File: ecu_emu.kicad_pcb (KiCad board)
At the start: 2 copper layers, 51.3 x 16.5 mm, 34 parts, among them J1 Conn_02x06_Odd_Even, J2 Conn_01x04_Male, U1 LD1117S33TR_SOT223, U2 STM32F105RBTx, U3 BSP742R, U4 E-L9637D, Y1 Crystal KX-9A

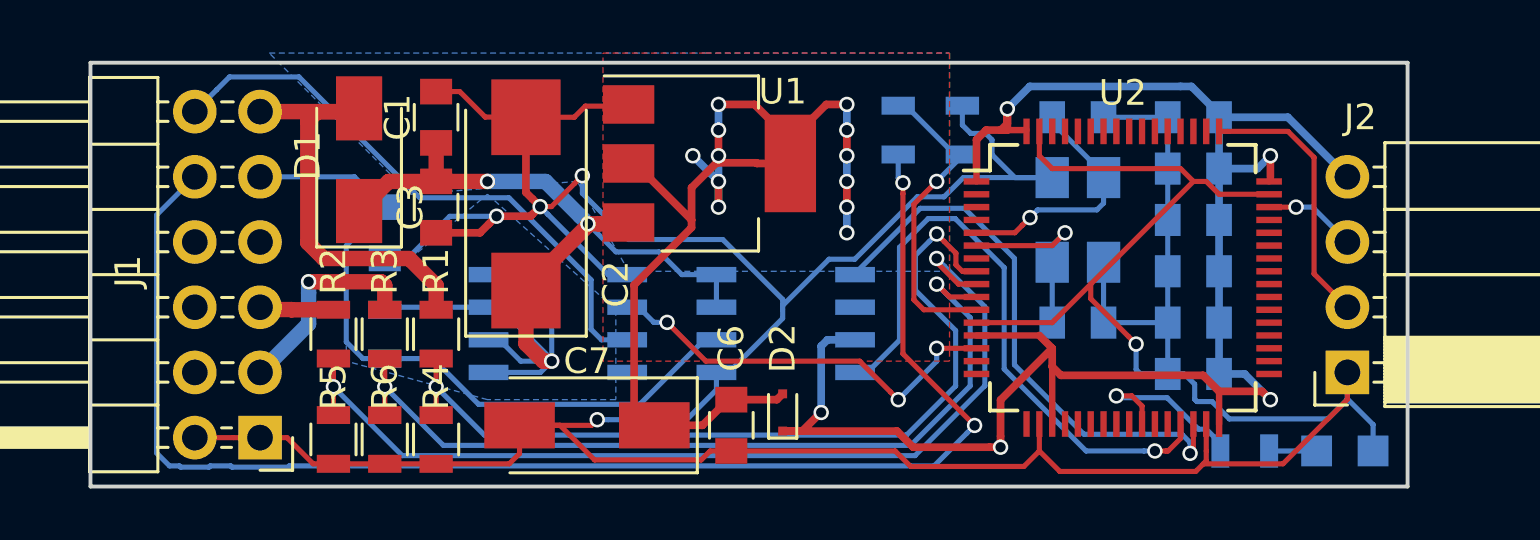
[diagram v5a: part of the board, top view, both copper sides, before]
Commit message: more fixes 1. separate power on k-bus IC logic 2. D2 change to shottky diod 3. pull-up on stm RESET pin 4. change linier stabilizer to adjastable version, to make apropriate voltage on stm throw diod
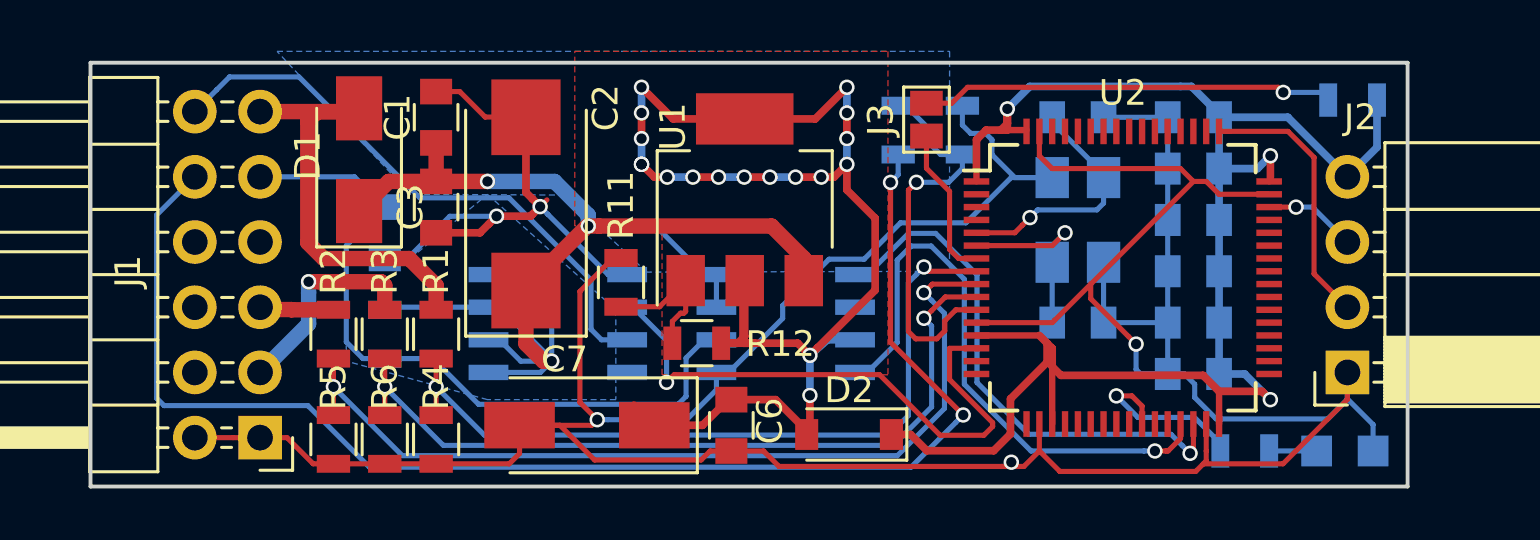
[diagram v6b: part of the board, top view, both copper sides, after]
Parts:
- added J3: GS2, Connectors:GS2, F.Cu at (60.6, 23.1)
- added R11: 240, Resistors_SMD:R_0805, F.Cu at (48.7, 29.4)
- added R12: 120, Resistors_SMD:R_0805, F.Cu at (51.7, 31.8)
- added R13: 100k, Resistors_SMD:R_0805, B.Cu at (77.2, 22.3)
- D2: value PMLL4148L.115 -> 1N5819HW-7-F; footprint Diodes_SMD:D_SC-80 -> Diodes_SMD:D_SOD-123
- U1: value LD1117S33TR_SOT223 -> AMS1117-ADJ
- moved D2 2.72 mm to (57.6, 35.4), turned to 180 degrees
- moved U1 1.97 mm to (53.5, 26.2), turned to 90 degrees
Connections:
- J1 pad 4: /ECU_P/N -> (no net)
- J1 pad 6: Net-(J1-Pad6) -> (no net)
- J1 pad 7: Net-(J1-Pad7) -> (no net)
- J1 pad 8: /Transmission_control_module -> (no net)
- U1 pad 1: GND -> Net-(R11-Pad1)
- U2 pad 15: Net-(U2-Pad15) -> (no net)
- U2 pad 16: Net-(U2-Pad16) -> (no net)
- U2 pad 17: Net-(U2-Pad17) -> (no net)
- U2 pad 2: Net-(U2-Pad2) -> (no net)
- U2 pad 20: Net-(U2-Pad20) -> (no net)
- U2 pad 21: Net-(U2-Pad21) -> (no net)
- U2 pad 22: Net-(U2-Pad22) -> (no net)
- U2 pad 23: Net-(U2-Pad23) -> (no net)
- U2 pad 24: Net-(U2-Pad24) -> (no net)
- U2 pad 25: Net-(U2-Pad25) -> (no net)
- U2 pad 27: Net-(U2-Pad27) -> (no net)
- U2 pad 28: Net-(U2-Pad28) -> (no net)
- U2 pad 3: Net-(U2-Pad3) -> (no net)
- U2 pad 33: Net-(U2-Pad33) -> (no net)
- U2 pad 34: Net-(U2-Pad34) -> (no net)
- U2 pad 35: Net-(U2-Pad35) -> (no net)
- U2 pad 36: Net-(U2-Pad36) -> (no net)
- U2 pad 37: Net-(U2-Pad37) -> (no net)
- U2 pad 38: Net-(U2-Pad38) -> (no net)
- U2 pad 39: Net-(U2-Pad39) -> (no net)
- U2 pad 4: Net-(U2-Pad4) -> (no net)
- U2 pad 40: Net-(U2-Pad40) -> (no net)
- U2 pad 41: Net-(U2-Pad41) -> (no net)
- U2 pad 42: Net-(U2-Pad42) -> (no net)
- U2 pad 43: Net-(U2-Pad43) -> (no net)
- U2 pad 44: Net-(U2-Pad44) -> (no net)
- U2 pad 45: Net-(U2-Pad45) -> (no net)
- U2 pad 50: Net-(U2-Pad50) -> (no net)
- U2 pad 51: Net-(U2-Pad51) -> (no net)
- U2 pad 52: Net-(U2-Pad52) -> (no net)
- U2 pad 53: Net-(U2-Pad53) -> (no net)
- U2 pad 54: Net-(U2-Pad54) -> (no net)
- U2 pad 55: Net-(U2-Pad55) -> (no net)
- U2 pad 56: Net-(U2-Pad56) -> (no net)
- U2 pad 57: Net-(U2-Pad57) -> (no net)
- U2 pad 58: Net-(U2-Pad58) -> (no net)
- U2 pad 59: Net-(U2-Pad59) -> (no net)
- U2 pad 60: Net-(U2-Pad60) -> (no net)
- U2 pad 61: Net-(U2-Pad61) -> (no net)
- U2 pad 62: Net-(U2-Pad62) -> (no net)
- U2 pad 7: Net-(U2-Pad7) -> /NRST
- U3 pad 4: Net-(U3-Pad4) -> (no net)
- U4 pad 2: Net-(U4-Pad2) -> (no net)
- U4 pad 3: /+3V3_STM -> /+3V3
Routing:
- net Net-(J3-Pad2): track 0.00 -> 16.1 mm, vias 0 -> 1
- net /+3V3: track 42.1 -> 55.4 mm, vias 12 -> 18
- net GND: track 179.6 -> 171.0 mm
- net /Kbus_Vbatt: track 44.8 -> 53.2 mm
- net /+3V3_STM: track 72.9 -> 66.4 mm, vias 5 -> 3
- net /solenoid_driver: track 16.2 -> 22.4 mm, vias 3 -> 1
- net Net-(R11-Pad1): track 0.00 -> 6.14 mm
- net /NRST: track 0.00 -> 5.98 mm
- net /ADC_Vbatt: track 33.3 -> 29.8 mm
- net Net-(R7-Pad1): track 12.3 -> 15.6 mm
- net /ADC_IGN: track 37.6 -> 34.9 mm
- net /ADC_AUX: track 33.2 -> 31.0 mm
- net /ECU_HALL_sensor+: track 56.0 -> 54.1 mm
- net /stm2Kbus_UART_RX: track 22.0 -> 20.9 mm
- net /stm2Kbus_UART_TX: track 24.1 -> 23.1 mm
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
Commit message: fix some, update gerbers
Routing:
- net /solenoid_driver: track 22.4 -> 23.2 mm
- net GND: track 171.0 -> 171.7 mm
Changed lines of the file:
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@@
     (thickness 1.6)
     (drawings 10)
-    (tracks 492)
+    (tracks 500)
     (zones 0)
     (modules 38)
@@
     (last_trace_width 0.2)
     (trace_clearance 0.2)
-    (zone_clearance 0.4)
+    (zone_clearance 0.45)
     (zone_45_only yes)
     (trace_min 0.1)
@@
       (padsonsilk false)
       (subtractmaskfromsilk false)
-      (outputformat 4)
+      (outputformat 1)
       (mirror false)
       (drillshape 0)
@@
   (gr_line (start 28.036 20.875) (end 79.344 20.875) (layer Edge.Cuts) (width 0.15))
   (gr_line (start 28.036 37.385) (end 28.036 20.875) (layer Edge.Cuts) (width 0.15))
+  (segment (start 34.64 35.48) (end 35.929969 35.48) (width 0.2) (layer F.Cu) (net 1))
+  (segment (start 35.929969 35.48) (end 36.17916 35.729191) (width 0.2) (layer F.Cu) (net 1))
+  (segment (start 36.17916 35.729191) (end 36.17916 36.374) (width 0.2) (layer F.Cu) (net 1))
+  (segment (start 36.30516 36.5) (end 37.5 36.5) (width 0.2) (layer F.Cu) (net 1))
+  (segment (start 36.17916 36.374) (end 36.30516 36.5) (width 0.2) (layer F.Cu) (net 1))
+  (segment (start 48.702 28.482) (end 48.702 29.256) (width 0.2) (layer F.Cu) (net 1))
+  (segment (start 48.702 29.256) (end 48.501436 29.456564) (width 0.2) (layer F.Cu) (net 1))
+  (segment (start 48.501436 29.456564) (end 47.788188 29.456564) (width 0.2) (layer F.Cu) (net 1))
+  (segment (start 47.788188 29.456564) (end 47.102 30.142752) (width 0.2) (layer F.Cu) (net 1))
+  (segment (start 47.102 30.142752) (end 47.102 34.107267) (width 0.2) (layer F.Cu) (net 1))
+  (segment (start 47.102 34.107267) (end 47.776239 34.781506) (width 0.2) (layer F.Cu) (net 1))
   (segment (start 63.502 36.603056) (end 64.396944 36.603056) (width 0.2) (layer F.Cu) (net 1))
   (segment (start 54.859656 36.603056) (end 63.502 36.603056) (width 0.2) (layer F.Cu) (net 1))
@@
   (segment (start 62.137598 27.112716) (end 63.902 25.348314) (width 0.2) (layer B.Cu) (net 1))
   (segment (start 65.498314 25.348314) (end 65.5 25.35) (width 0.2) (layer B.Cu) (net 1))
-  (segment (start 47.102 29.782) (end 47.102 34.107267) (width 0.2) (layer F.Cu) (net 1))
-  (segment (start 48.402 28.482) (end 47.102 29.782) (width 0.2) (layer F.Cu) (net 1))
-  (segment (start 47.102 34.107267) (end 47.776239 34.781506) (width 0.2) (layer F.Cu) (net 1))
-  (segment (start 48.702 28.482) (end 48.402 28.482) (width 0.2) (layer F.Cu) (net 1))
   (segment (start 77 32.94) (end 77 33.99) (width 0.2) (layer B.Cu) (net 1))
   (segment (start 77 33.99) (end 76.239037 34.750963) (width 0.2) (layer B.Cu) (net 1))
@@
   (segment (start 44.991758 22.991758) (end 45 23) (width 0.2) (layer F.Cu) (net 1))
   (segment (start 43.412329 22.991758) (end 44.991758 22.991758) (width 0.2) (layer F.Cu) (net 1))
-  (segment (start 34.64 35.48) (end 35.69 35.48) (width 0.2) (layer F.Cu) (net 1))
-  (segment (start 35.69 35.48) (end 36.71 36.5) (width 0.2) (layer F.Cu) (net 1))
-  (segment (start 36.71 36.5) (end 37.5 36.5) (width 0.2) (layer F.Cu) (net 1))
   (segment (start 71 25.5) (end 67 29.5) (width 0.2) (layer F.Cu) (net 1))
   (segment (start 67 29.5) (end 65.600009 30.899991) (width 0.2) (layer F.Cu) (net 1))
@@
   (segment (start 34.64 22.78) (end 38.373 22.78) (width 0.6) (layer F.Cu) (net 6))
   (segment (start 38.373 22.78) (end 38.5 22.653) (width 0.6) (layer F.Cu) (net 6))
+  (segment (start 63.752992 22.672254) (end 63.752992 23.24967) (width 0.3) (layer F.Cu) (net 7))
+  (segment (start 63.752992 23.24967) (end 63.502662 23.5) (width 0.3) (layer F.Cu) (net 7))
+  (segment (start 63.502662 23.5) (end 63.5 23.5) (width 0.3) (layer F.Cu) (net 7))
   (segment (start 78.152 22.332) (end 78.152 24.168) (width 0.3) (layer B.Cu) (net 7))
   (segment (start 78.152 24.168) (end 77 25.32) (width 0.3) (layer B.Cu) (net 7))
@@
   (segment (start 74.68 23) (end 72 23) (width 0.3) (layer B.Cu) (net 7))
   (segment (start 63.5 23.5) (end 64.5 23.5) (width 0.25) (layer F.Cu) (net 7))
-  (segment (start 63.752992 23.247008) (end 63.5 23.5) (width 0.3) (layer F.Cu) (net 7))
-  (segment (start 63.752992 22.672254) (end 63.752992 23.247008) (width 0.3) (layer F.Cu) (net 7))
   (segment (start 72 33) (end 72.997452 33) (width 0.3) (layer B.Cu) (net 7))
   (segment (start 72.997452 33) (end 73.998414 34.000962) (width 0.3) (layer B.Cu) (net 7))
@@
   (segment (start 62.55 30.5) (end 61.747516 30.5) (width 0.2) (layer F.Cu) (net 16))
   (segment (start 59.5 22.55) (end 59.8 22.55) (width 0.2) (layer B.Cu) (net 16))
-  (segment (start 61.5 32) (end 61.5 33.215499) (width 0.2) (layer F.Cu) (net 17))
-  (segment (start 61.5 33.215499) (end 63.180829 34.896328) (width 0.2) (layer F.Cu) (net 17))
+  (segment (start 63.180829 34.896328) (end 63.180829 35.046608) (width 0.2) (layer F.Cu) (net 17))
   (segment (start 63.180829 35.046608) (end 62.838522 35.388915) (width 0.2) (layer F.Cu) (net 17))
+  (segment (start 62.118501 33.834) (end 63.180829 34.896328) (width 0.2) (layer F.Cu) (net 17))
+  (segment (start 60.888 32.818) (end 61.904 33.834) (width 0.2) (layer F.Cu) (net 17))
+  (segment (start 61.198 32) (end 60.888 32.31) (width 0.2) (layer F.Cu) (net 17))
+  (segment (start 60.888 32.31) (end 60.888 32.818) (width 0.2) (layer F.Cu) (net 17))
+  (segment (start 62.55 32) (end 61.198 32) (width 0.2) (layer F.Cu) (net 17))
+  (segment (start 61.904 33.834) (end 62.118501 33.834) (width 0.2) (layer F.Cu) (net 17))
   (segment (start 50.776469 33.025666) (end 50.47647 33.325665) (width 0.2) (layer F.Cu) (net 17))
-  (segment (start 63.180829 34.896328) (end 63.180829 35.046608) (width 0.2) (layer F.Cu) (net 17))
   (segment (start 62.838522 35.388915) (end 61.133893 35.388915) (width 0.2) (layer F.Cu) (net 17))
   (segment (start 61.133893 35.388915) (end 58.770644 33.025666) (width 0.2) (layer F.Cu) (net 17))
@@
   (via (at 50.47647 33.325665) (size 0.6) (drill 0.4) (layers F.Cu B.Cu) (net 17))
   (segment (start 49.177561 30.4) (end 50.47647 31.698909) (width 0.2) (layer B.Cu) (net 17))
-  (segment (start 61.5 32) (end 62.55 32) (width 0.2) (layer F.Cu) (net 17))
   (segment (start 45 29.625) (end 47.386584 27.238416) (width 0.6) (layer F.Cu) (net 18))
   (segment (start 45 29.75) (end 45 29.625) (width 0.6) (layer F.Cu) (net 18))
@@
   (segment (start 39.653 25.5) (end 38.5 26.653) (width 0.6) (layer F.Cu) (net 18))
   (segment (start 41.5 24) (end 41.5 25.5) (width 0.6) (layer F.Cu) (net 18))
+  (segment (start 38 28) (end 39.5 26.5) (width 0.2) (layer B.Cu) (net 19))
+  (segment (start 38 31.75) (end 38 28) (width 0.2) (layer B.Cu) (net 19))
+  (segment (start 38.65 32.4) (end 38 31.75) (width 0.2) (layer B.Cu) (net 19))
+  (segment (start 39.5 32.4) (end 38.65 32.4) (width 0.2) (layer B.Cu) (net 19))
   (segment (start 52.42 31.67) (end 51.945 31.67) (width 0.2) (layer B.Cu) (net 19))
   (segment (start 51.945 31.67) (end 51.236154 32.378846) (width 0.2) (layer B.Cu) (net 19))
@@
   (segment (start 39.498685 26.5) (end 38.318685 25.32) (width 0.2) (layer B.Cu) (net 19))
   (segment (start 38.318685 25.32) (end 34.64 25.32) (width 0.2) (layer B.Cu) (net 19))
-  (segment (start 38 28) (end 39.5 26.5) (width 0.2) (layer B.Cu) (net 19))
-  (segment (start 38 31.75) (end 38 28) (width 0.2) (layer B.Cu) (net 19))
-  (segment (start 39.5 32.4) (end 38.65 32.4) (width 0.2) (layer B.Cu) (net 19))
-  (segment (start 38.65 32.4) (end 38 31.75) (width 0.2) (layer B.Cu) (net 19))
   (segment (start 39.2 32.4) (end 39.5 32.4) (width 0.2) (layer B.Cu) (net 19))
   (segment (start 34.96 25) (end 34.64 25.32) (width 0.2) (layer B.Cu) (net 19))
@@
   (segment (start 62.202 21.832) (end 61.582 22.452) (width 0.2) (layer F.Cu) (net 25))
   (segment (start 61.582 22.452) (end 60.602 22.452) (width 0.2) (layer F.Cu) (net 25))
-  (segment (start 51.022 30.632) (end 51.154 30.632) (width 0.2) (layer F.Cu) (net 26))
-  (segment (start 51.154 30.632) (end 51.222 30.564) (width 0.2) (layer F.Cu) (net 26))
-  (segment (start 51.222 30.564) (end 51.222 29.364) (width 0.2) (layer F.Cu) (net 26))
   (segment (start 50.702 31.802) (end 50.702 30.952) (width 0.2) (layer F.Cu) (net 26))
-  (segment (start 50.702 30.952) (end 51.022 30.632) (width 0.2) (layer F.Cu) (net 26))
+  (segment (start 50.702 30.952) (end 51.223076 30.430924) (width 0.2) (layer F.Cu) (net 26))
+  (segment (start 51.223076 30.430924) (end 51.223076 30.34733) (width 0.2) (layer F.Cu) (net 26))
+  (segment (start 51.223076 30.34733) (end 51.222 30.346254) (width 0.2) (layer F.Cu) (net 26))
+  (segment (start 51.222 30.346254) (end 51.222 29.364) (width 0.2) (layer F.Cu) (net 26))
   (segment (start 48.702 30.382) (end 50.204 30.382) (width 0.2) (layer F.Cu) (net 26))
   (segment (start 50.204 30.382) (end 51.222 29.364) (width 0.2) (layer F.Cu) (net 26))
